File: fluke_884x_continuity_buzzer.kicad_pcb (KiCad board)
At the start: 4 copper layers, 67.4 x 71.4 mm, 70 parts, among them J2 Conn_01x02, J203 16 pin DIP socket, J204 16 pin DIP socket, J3 USB_B_Micro, P203 16 pin DIP plug, P204 16 pin DIP plug, U1 NCP1117-3.3_SOT223, U2 W25Q128JVS, U3 RP2040, Y1 ABLS-12.000MHZ-B4-T

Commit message: Added LCSC refs
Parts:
- added REF**: Symbol_CC-Noncommercial_CopperTop_Small, Symbol:Symbol_CC-Noncommercial_CopperTop_Small, F.Cu at (136.3, 29.4)
- J3: footprint RP2040_minimal:USB_Micro-B_Amphenol_10103594-0001LF_Horizontal_modified -> Connector_USB:USB_Micro-B_Amphenol_10118194_Horizontal
- U1: value NCP1117-3.3_SOT223 -> AZ117EH-3.3
- moved J3 0.94 mm to (138.3, 86.4)
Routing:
- net GND: track 44.7 -> 54.7 mm, vias 34 -> 36
- net +3V3: track 114.3 -> 105.1 mm, vias 23 -> 21
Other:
- board text added: "Fluke 8840A/8842A Continuity Buzzer"
- board text added: "https://github.com/bikeNomad/fluke_884x_continuity_buzzer"

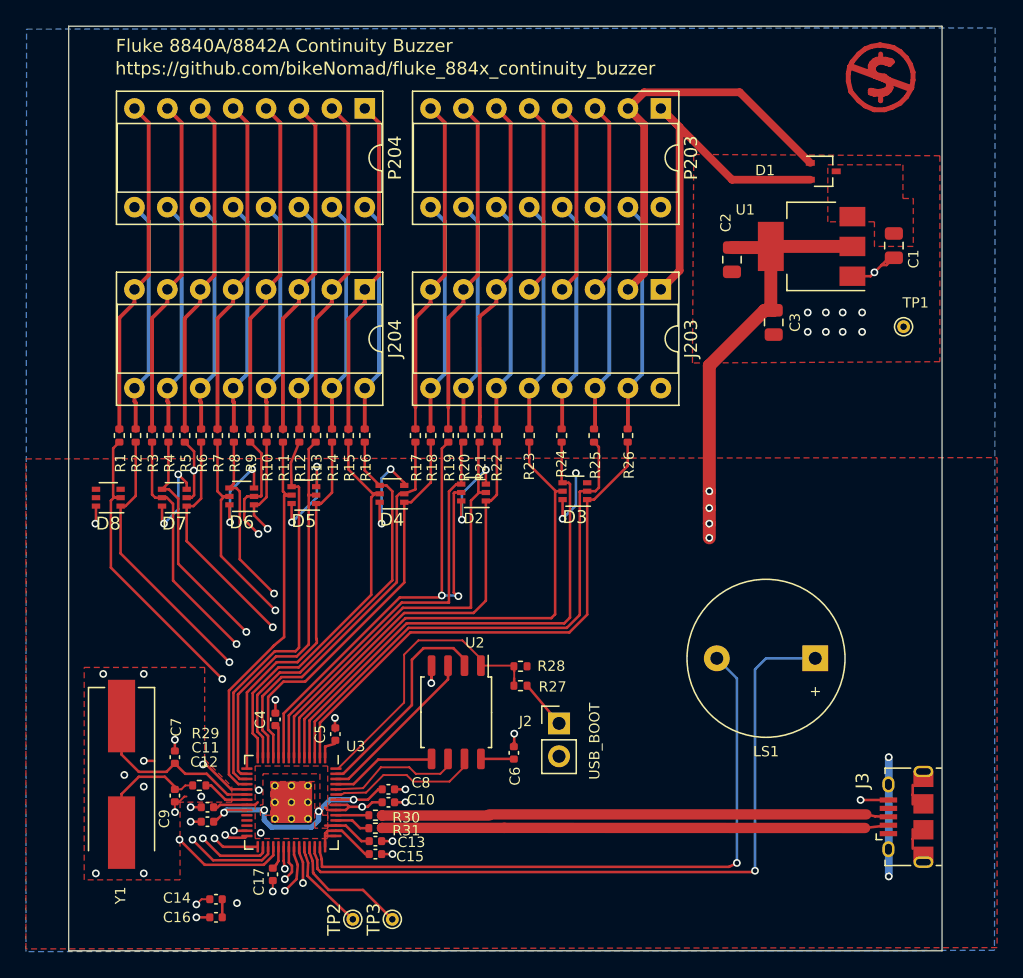
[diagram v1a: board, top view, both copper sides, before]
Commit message: Updated text; fixed silk
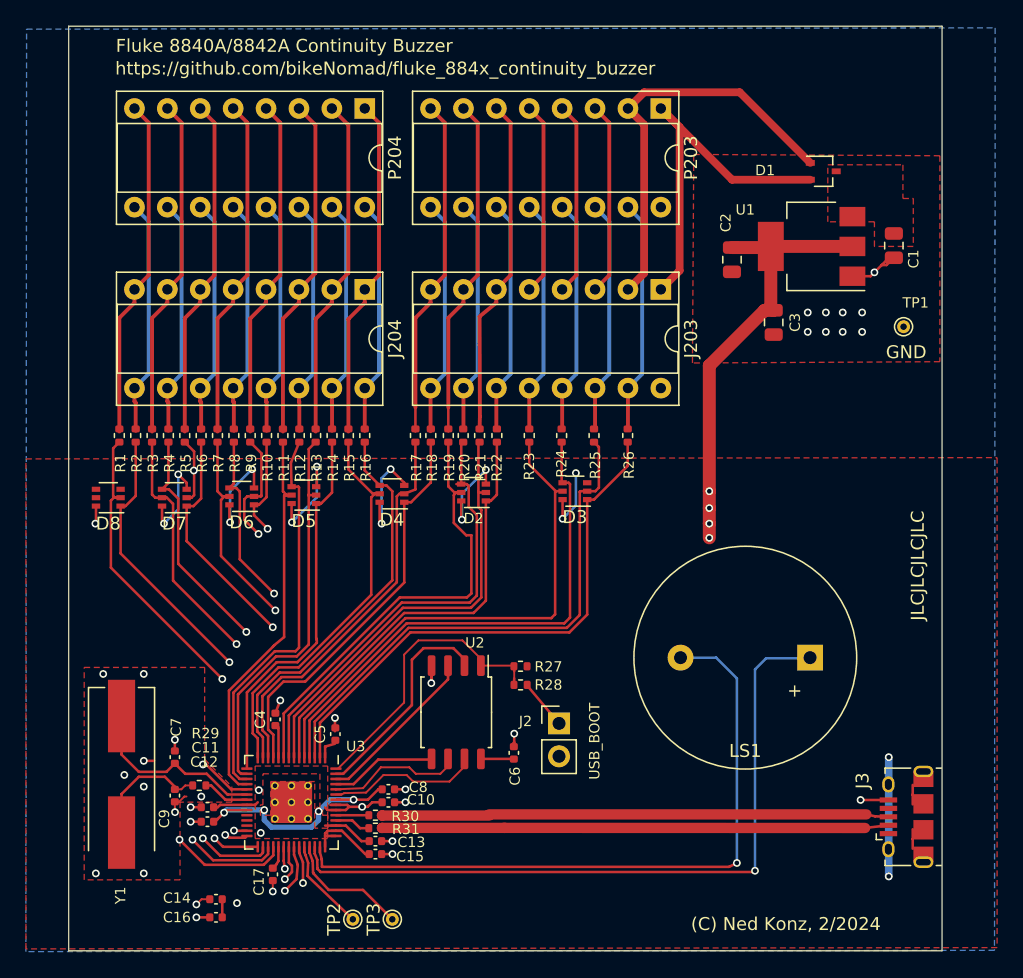
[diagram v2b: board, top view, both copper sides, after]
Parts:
- removed REF**: Symbol_CC-Noncommercial_CopperTop_Small, Symbol:Symbol_CC-Noncommercial_CopperTop_Small
- LS1: footprint Buzzer_Beeper:Buzzer_12x9.5RM7.6 -> RP2040_minimal:Buzzer_17x9RM10
- moved LS1 5.40 mm to (125.9, 74.2)
- moved R28 0.07 mm to (108.5, 76.2)
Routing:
- net G7_3V: track 41.1 -> 35.4 mm, vias 2 -> 0
- net /GPIO29_ADC3: track 50.1 -> 52.9 mm
- net RL1_3V: track 32.1 -> 34.4 mm
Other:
- board text added: "(C) Ned Konz, 2/2024"
- board text added: "JLCJLCJLCJLC"
